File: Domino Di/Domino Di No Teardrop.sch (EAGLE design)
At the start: 41 parts, among them J1 LiPo Battery, J2 MH28-1, J3 MH28-1, M1 DOMINO, SW1 IT-1210, U1 AMS1117-3.3, U2 MCP73831T-2ACI/OT

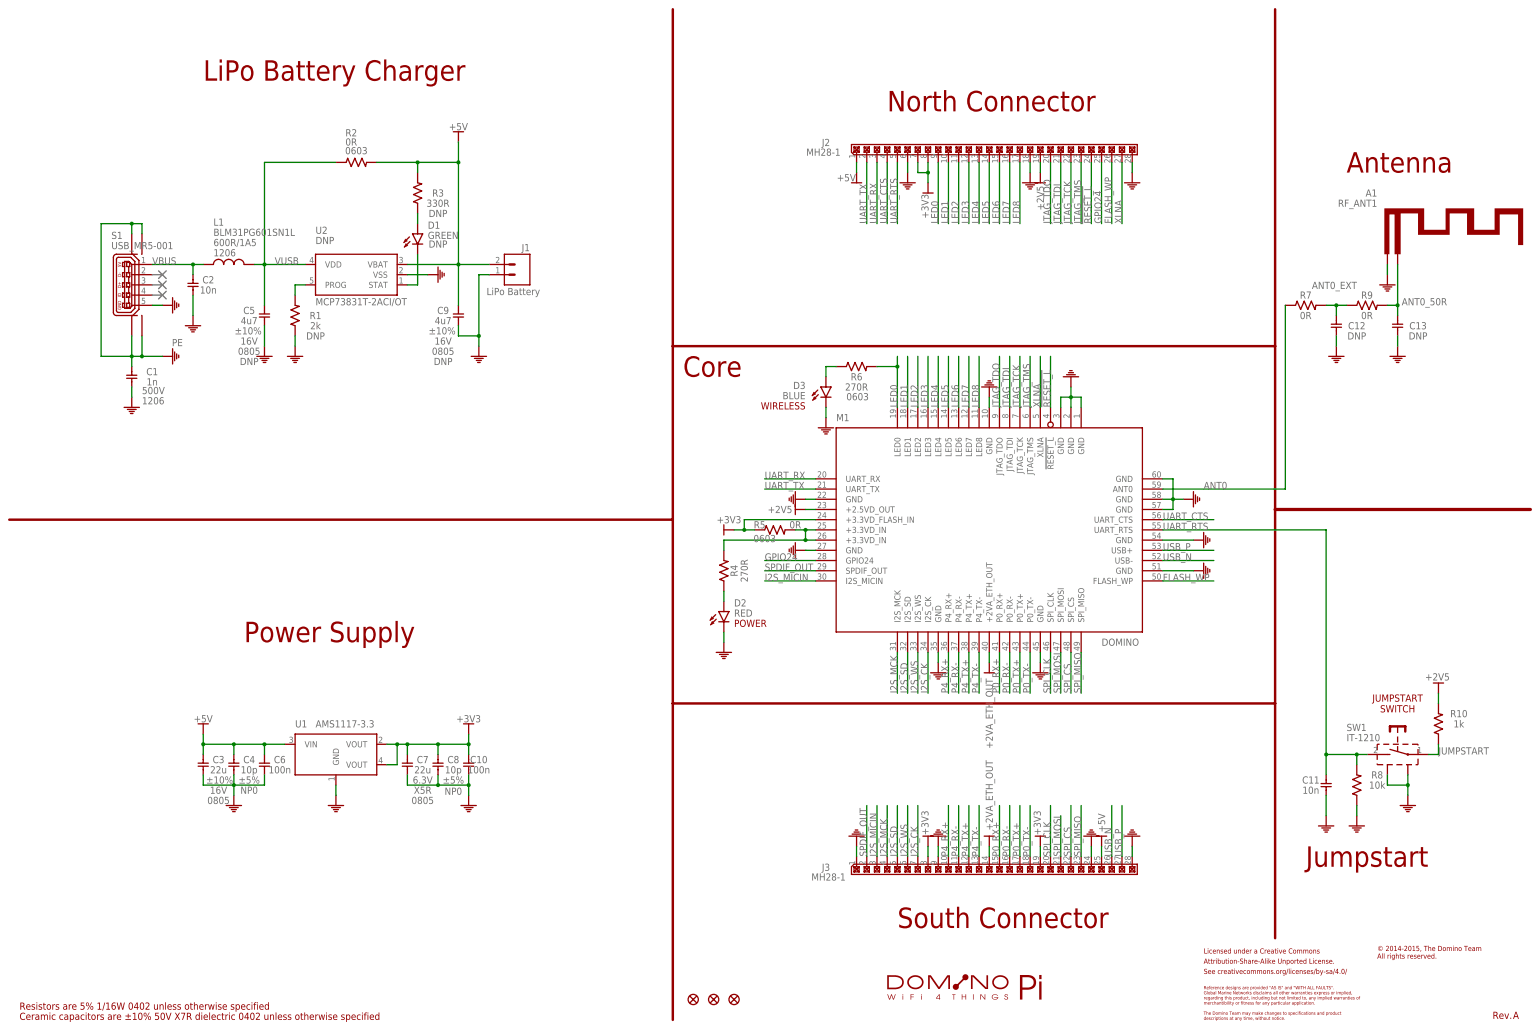
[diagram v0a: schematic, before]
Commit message: Domino Di Rev. A: added slider switch
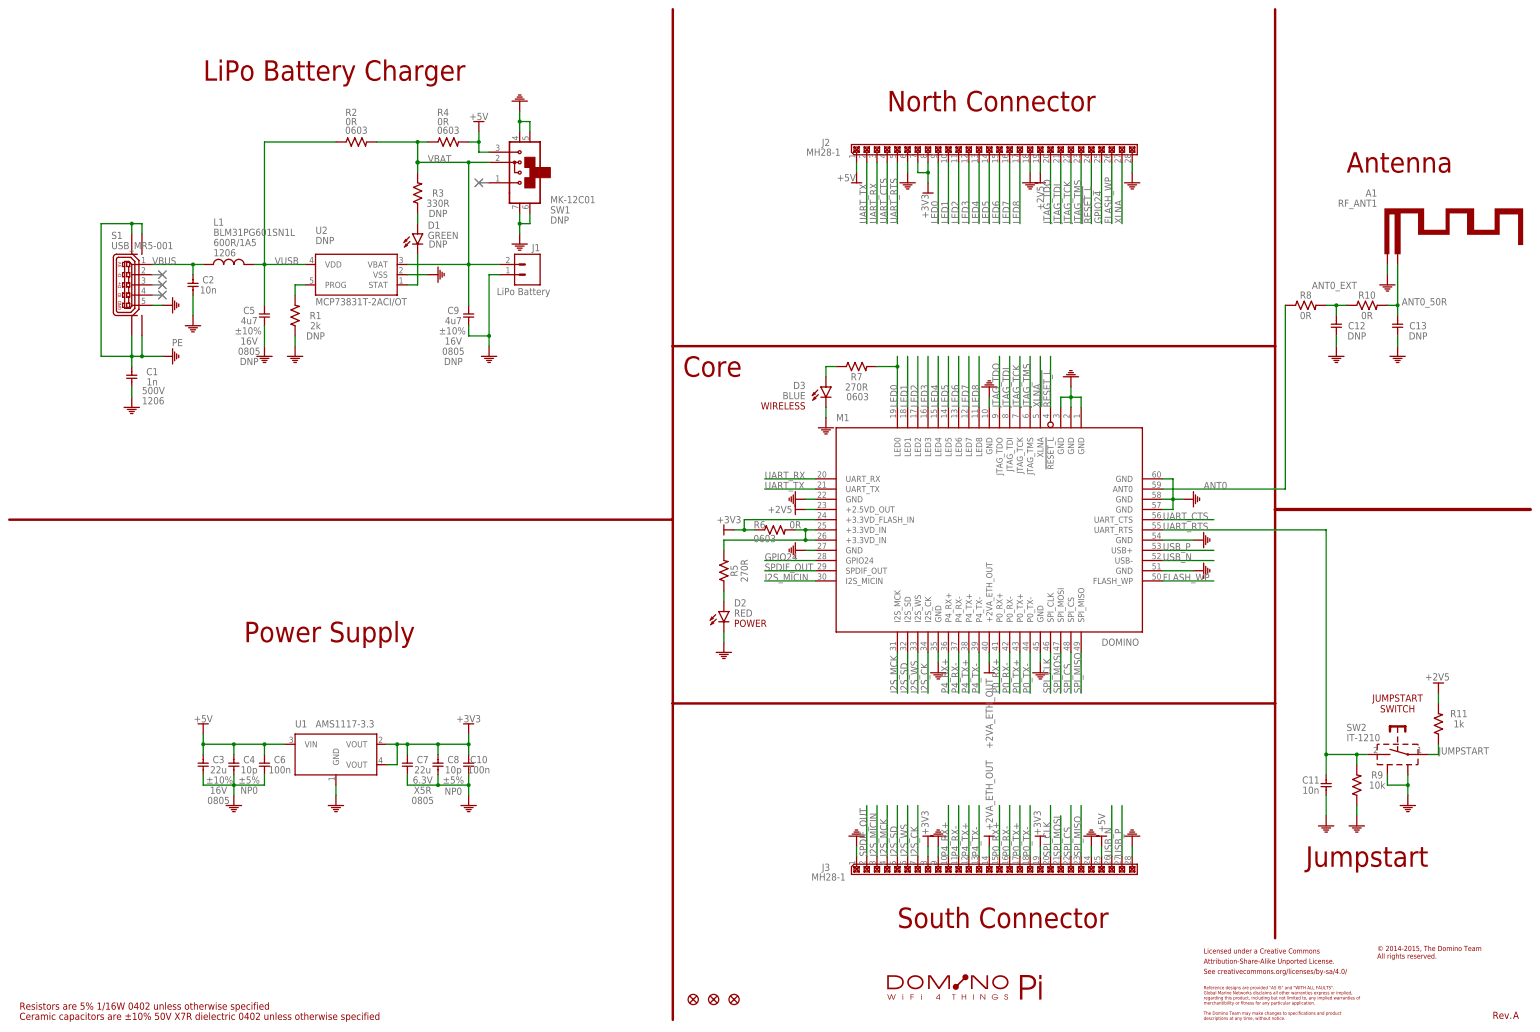
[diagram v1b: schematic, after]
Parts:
- added R11: 1k, Domino:RES_0402
- added SW2: IT-1210, Domino:IT-1210
- R10: value 1k -> 0R; PARTNO R0402_1k_5%_62.5mW -> R0402_0R_5%_62.5mW
- R4: value 270R -> 0R; device Domino:RES_0402 -> Domino:RES_0603; PARTNO R0402_270R_5%_62.5mW -> R0603_0R_5%_125mW; RATE 62.5mW -> 125mW
- R5: value 0R -> 270R; device Domino:RES_0603 -> Domino:RES_0402; PARTNO R0603_0R_5%_125mW -> R0402_270R_5%_62.5mW; RATE 125mW -> 62.5mW
- R6: value 270R -> 0R; PARTNO R0603_270R_5%_125mW -> R0603_0R_5%_125mW
- R7: value 0R -> 270R; device Domino:RES_0402 -> Domino:RES_0603; PARTNO R0402_0R_5%_62.5mW -> R0603_270R_5%_125mW; RATE 62.5mW -> 125mW
- R8: value 10k -> 0R; PARTNO R0402_10k_5%_62.5mW -> R0402_0R_5%_62.5mW
- R9: value 0R -> 10k; PARTNO R0402_0R_5%_62.5mW -> R0402_10k_5%_62.5mW
- SW1: value IT-1210 -> MK-12C01; device Domino:IT-1210 -> Domino:MK-12C01; DNP (none) -> T; PARTNO IT-1210 -> MK-12C01; RATE (none) -> 0.3A; VOLT (none) -> 6V
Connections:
- new net VBAT: C9.1, J1.2, R2.2, R3.2, R4.1, SW1.2, U2.VBAT
- net +2V5: now also R11.2; no longer R10.2
- net +3.3VD_IN: now also R6.2; no longer R4.2
- net +3V3: now also R6.1; no longer R5.1
- net +5V: now also R4.2, SW1.3; no longer C9.1, J1.2, R2.2, R3.2, U2.VBAT
- net ANT0: now also R8.1; no longer R7.1
- net ANT0_50R: now also R10.2; no longer R9.2
- net ANT0_EXT: now also R10.1, R8.2; no longer R7.2, R9.1
- net BLUE_LED: now also R7.1; no longer R6.1
- net GND: now also R9.1, SW1.4, SW1.5, SW1.6, SW1.7, SW2.SH$1, SW2.SH$2; no longer R8.1, SW1.SH$1, SW1.SH$2
- net JUMPSTART: now also R11.1, SW2.1; no longer R10.1, SW1.1
- net LED0: now also R7.2; no longer R6.2
- net N$1: now also R5.1; no longer R4.1
- net UART_RTS: now also R9.2, SW2.2; no longer R8.2, SW1.2
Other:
- moved on the sheet: C9, J1, R10, R2, R4, R5, R6, R7, R8, R9

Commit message: Domino Di Rev. B: removed battery charger as too complex
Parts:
- removed C1: 1n, Domino:CAP_1206
- removed C2: 10n, Domino:CAP_0402
- removed C5, C9: 4u7, Domino:CAP_0805
- removed D1: GREEN, Domino:LED_0402
- removed L1: BLM31PG601SN1L, Domino:FB_1206
- removed R1: 2k, Domino:RES_0402
- removed R2, R4: 0R, Domino:RES_0603
- removed R3: 330R, Domino:RES_0402
- removed SW1: MK-12C01, Domino:MK-12C01
- removed U2: MCP73831T-2ACI/OT, Domino:MCP73831T-2ACI/OT
- R7: device Domino:RES_0603 -> Domino:RES_0402; PARTNO R0603_270R_5%_125mW -> R0402_270R_5%_62.5mW; RATE 125mW -> 62.5mW
- W1: value DOMINO_PI_LOGO -> DOMINO_LOGO; device Domino:DOMINO_PI_LOGO -> Domino:DOMINO_LOGO
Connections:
- removed net N$2: D1.C, U2.STAT
- removed net N$3: D1.A, R3.1
- removed net N$5: R1.2, U2.PROG
- removed net PE: C1.1, S1.M0, S1.M1, S1.M2, S1.M3
- removed net VBAT: C9.1, J1.2, R2.2, R3.2, R4.1, SW1.2, U2.VBAT
- removed net VBUS: C2.1, L1.2, S1.1
- removed net VUSB: C5.1, L1.1, R2.1, U2.VDD
- net +5V: now also J1.2, S1.1; no longer R4.2, SW1.3
- net GND: now also S1.M0, S1.M1, S1.M2, S1.M3; no longer C1.2, C2.2, C5.2, C9.2, R1.1, SW1.4, SW1.5, SW1.6, SW1.7, U2.VSS
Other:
- note removed: "LiPo Battery Charger"
- moved on the sheet: C10, C3, C4, C6, C7, C8, J1, S1, U1
